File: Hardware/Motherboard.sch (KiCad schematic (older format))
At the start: 41 parts, among them J1 Pin_Header_02x08, J2 Pin_Header_02x08, J3 Pin_Header_02x08, J4 USB_B_Mini, J5 JTAG, SW1 SW_SPDT, U1 PIC18F26K22-I-SO, U2 FT240XS, U3 TXB0104D, U4 TXB0104D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

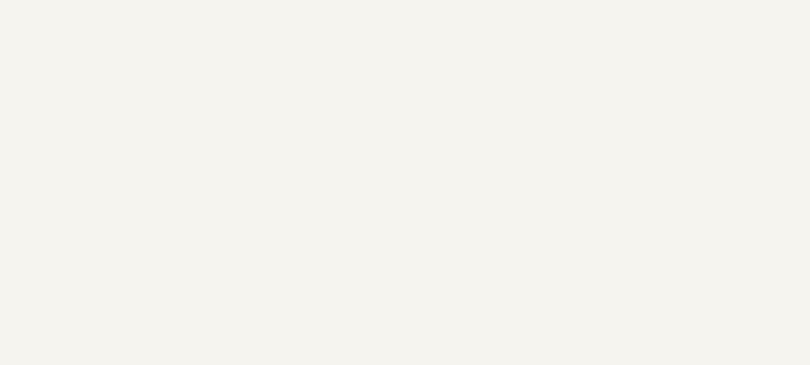
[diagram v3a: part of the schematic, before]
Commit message: [Hardware] Added PCB mounting holes.
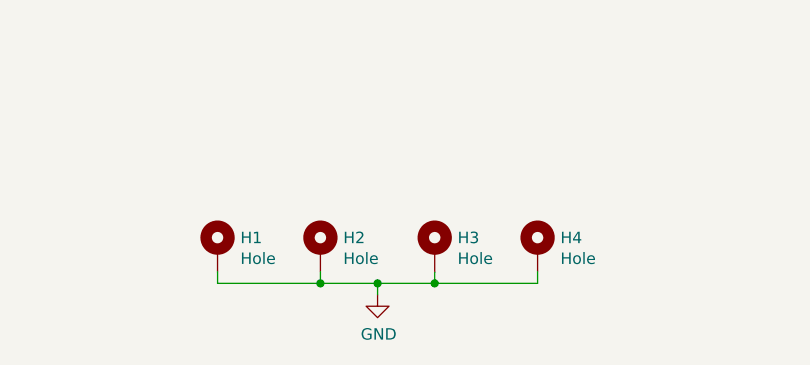
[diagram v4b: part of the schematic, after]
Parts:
- added H1, H2, H3, H4: Hole, MountingHole:MountingHole_3mm_Pad, symbol Mechanical:MountingHole_Pad
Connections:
- net GND: now also H1.1, H2.1, H3.1, H4.1
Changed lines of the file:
@@
 Text Notes 13800 6300 0    50   ~ 0
 Select logic signals voltage.
+$Comp
+L Mechanical:MountingHole_Pad H1
+U 1 1 5F6BD5D3
+P 7250 9850
+F 0 "H1" H 7350 9899 50  0000 L CNN
+F 1 "Hole" H 7350 9808 50  0000 L CNN
+F 2 "MountingHole:MountingHole_3mm_Pad" H 7250 9850 50  0001 C CNN
+F 3 "~" H 7250 9850 50  0001 C CNN
+	1    7250 9850
+	1    0    0    -1
+$EndComp
+$Comp
+L power:GND #PWR039
+U 1 1 5F6BDC13
+P 7950 10050
+F 0 "#PWR039" H 7950 9800 50  0001 C CNN
+F 1 "GND" H 7955 9877 50  0000 C CNN
+F 2 "" H 7950 10050 50  0001 C CNN
+F 3 "" H 7950 10050 50  0001 C CNN
+	1    7950 10050
+	1    0    0    -1
+$EndComp
+$Comp
+L Mechanical:MountingHole_Pad H2
+U 1 1 5F6E69A0
+P 7700 9850
+F 0 "H2" H 7800 9899 50  0000 L CNN
+F 1 "Hole" H 7800 9808 50  0000 L CNN
+F 2 "MountingHole:MountingHole_3mm_Pad" H 7700 9850 50  0001 C CNN
+F 3 "~" H 7700 9850 50  0001 C CNN
+	1    7700 9850
+	1    0    0    -1
+$EndComp
+$Comp
+L Mechanical:MountingHole_Pad H3
+U 1 1 5F6E6B58
+P 8200 9850
+F 0 "H3" H 8300 9899 50  0000 L CNN
+F 1 "Hole" H 8300 9808 50  0000 L CNN
+F 2 "MountingHole:MountingHole_3mm_Pad" H 8200 9850 50  0001 C CNN
+F 3 "~" H 8200 9850 50  0001 C CNN
+	1    8200 9850
+	1    0    0    -1
+$EndComp
+$Comp
+L Mechanical:MountingHole_Pad H4
+U 1 1 5F6E6DFE
+P 8650 9850
+F 0 "H4" H 8750 9899 50  0000 L CNN
+F 1 "Hole" H 8750 9808 50  0000 L CNN
+F 2 "MountingHole:MountingHole_3mm_Pad" H 8650 9850 50  0001 C CNN
+F 3 "~" H 8650 9850 50  0001 C CNN
+	1    8650 9850
+	1    0    0    -1
+$EndComp
+Wire Wire Line
+	7250 9950 7250 10000
+Wire Wire Line
+	7250 10000 7700 10000
+Wire Wire Line
+	7700 10000 7700 9950
+Wire Wire Line
+	7700 10000 7950 10000
+Wire Wire Line
+	7950 10000 7950 10050
+Connection ~ 7700 10000
+Connection ~ 7950 10000
+Wire Wire Line
+	7950 10000 8200 10000
+Wire Wire Line
+	8200 9950 8200 10000
+Connection ~ 8200 10000
+Wire Wire Line
+	8650 10000 8650 9950
+Wire Wire Line
+	8200 10000 8650 10000
 $EndSCHEMATC

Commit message: [Hardware] Started PCB routing. Switched to 4 layers to have power supply planes.
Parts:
- R2, R3: footprint Resistor_SMD:R_1206_3216Metric_Pad1.42x1.75mm_HandSolder -> Resistor_SMD:R_0805_2012Metric_Pad1.15x1.40mm_HandSolder
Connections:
- net USB_2_D-: now reaches R3.1, U2.13 (USBDP)
- net USB_2_D+: now reaches R2.1, U2.14 (USBDM)
- net USB_1_D-: now reaches C15.1, J4.2 (D-), R2.2
- net USB_1_D+: now reaches C16.1, J4.3 (D+), R3.2
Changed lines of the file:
@@
 Connection ~ 5200 9050
-$Comp
-L Device:R R?
-U 1 1 5F097AC5
-P 3850 2800
-AR Path="/5E7ACE5B/5F097AC5" Ref="R?"  Part="1"
-AR Path="/5F097AC5" Ref="R2"  Part="1"
-F 0 "R2" V 3553 2800 50  0000 C CNN
-F 1 "27" V 3644 2800 50  0000 C CNN
-F 2 "Resistor_SMD:R_1206_3216Metric_Pad1.42x1.75mm_HandSolder" V 3780 2800 50  0001 C CNN
-F 3 "~" H 3850 2800 50  0001 C CNN
-F 4 "1%" V 3735 2800 50  0000 C CNN "Value2"
-	1    3850 2800
-	0    1    1    0
-$EndComp
-$Comp
-L Device:R R?
-U 1 1 5F098F51
-P 3850 2900
-AR Path="/5E7ACE5B/5F098F51" Ref="R?"  Part="1"
-AR Path="/5F098F51" Ref="R3"  Part="1"
-F 0 "R3" V 3965 2900 50  0000 C CNN
-F 1 "27" V 4056 2900 50  0000 C CNN
-F 2 "Resistor_SMD:R_1206_3216Metric_Pad1.42x1.75mm_HandSolder" V 3780 2900 50  0001 C CNN
-F 3 "~" H 3850 2900 50  0001 C CNN
-F 4 "1%" V 4147 2900 50  0000 C CNN "Value2"
-	1    3850 2900
-	0    1    1    0
-$EndComp
 $Comp
 L power:+3.3VA #PWR028
@@
 Wire Wire Line
 	8200 10000 8650 10000
+Text Label 2500 2450 0    50   ~ 0
+USB_1_D+
+Text Label 2500 2550 0    50   ~ 0
+USB_1_D-
+Text Label 4200 2800 0    50   ~ 0
+USB_2_D+
+Text Label 4200 2900 0    50   ~ 0
+USB_2_D-
+$Comp
+L Device:R R?
+U 1 1 5F098F51
+P 3850 2900
+AR Path="/5E7ACE5B/5F098F51" Ref="R?"  Part="1"
+AR Path="/5F098F51" Ref="R3"  Part="1"
+F 0 "R3" V 3965 2900 50  0000 C CNN
+F 1 "27" V 4056 2900 50  0000 C CNN
+F 2 "Resistor_SMD:R_0805_2012Metric_Pad1.15x1.40mm_HandSolder" V 3780 2900 50  0001 C CNN
+F 3 "~" H 3850 2900 50  0001 C CNN
+F 4 "1%" V 4147 2900 50  0000 C CNN "Value2"
+	1    3850 2900
+	0    1    1    0
+$EndComp
+$Comp
+L Device:R R?
+U 1 1 5F097AC5
+P 3850 2800
+AR Path="/5E7ACE5B/5F097AC5" Ref="R?"  Part="1"
+AR Path="/5F097AC5" Ref="R2"  Part="1"
+F 0 "R2" V 3553 2800 50  0000 C CNN
+F 1 "27" V 3644 2800 50  0000 C CNN
+F 2 "Resistor_SMD:R_0805_2012Metric_Pad1.15x1.40mm_HandSolder" V 3780 2800 50  0001 C CNN
+F 3 "~" H 3850 2800 50  0001 C CNN
+F 4 "1%" V 3735 2800 50  0000 C CNN "Value2"
+	1    3850 2800
+	0    1    1    0
+$EndComp
 $EndSCHEMATC

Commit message: [Hardware] Finished PCB routing. Switched two schematic signals to help routing.
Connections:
- net FTDI_RD: now also U1.24 (RB3); no longer U1.23 (RB2)
- net FTDI_WR: now also U1.23 (RB2); no longer U1.24 (RB3)
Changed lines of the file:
@@
 Text Label 6750 3800 2    50   ~ 0
 FTDI_WR
+Text Label 12700 2800 2    50   ~ 0
+FTDI_RD
 Text Label 12700 2700 2    50   ~ 0
-FTDI_RD
-Text Label 12700 2800 2    50   ~ 0
 FTDI_WR
 Text Label 6750 3900 2    50   ~ 0
